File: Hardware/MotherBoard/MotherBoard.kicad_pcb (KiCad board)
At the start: 2 copper layers, 233.7 x 165.1 mm, 39 parts, among them J1 POWER, J10 I/O_PWR, J2 I/O0, J3 ISA00, J4 ISA10, J5 I/O1, J6 EXTRN_CLCK, J7 ISA01, J8 ISA11, J9 Conn_02x02_Odd_Even, SW1 SW_Push, U1 AMS1117-5.0, U2 28C256, U3 WD65C22, U4 HM62256BLP, U5 WD65C02, U6 4012, U7 4023, U8 4069, X1 ACO-1MHz

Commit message: Add buffers to extenstion ports
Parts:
- added U10: 74HCT541, Package_DIP:DIP-20_W7.62mm, F.Cu at (202.9, 26.7)
- added U11: SN74LVC245AN, Package_DIP:DIP-20_W7.62mm, F.Cu at (203.7, -35.6)
- added U12: SN74LVC245AN, Package_DIP:DIP-20_W7.62mm, F.Cu at (-40.9, -7.11)
- added U13: 74HCT541, Package_DIP:DIP-20_W7.62mm, F.Cu at (-39.9, 25.4)
- added U14: 74HCT541, Package_DIP:DIP-20_W7.62mm, F.Cu at (-41.1, -40.4)
- added U9: 74HCT541, Package_DIP:DIP-20_W7.62mm, F.Cu at (202.7, -5.08)
- moved Xiaoniuniu 217.4 mm to (37.6, 45.7)
- moved U2 101.2 mm to (128.8, 73.7)
- moved C6 101.2 mm to (146.8, 73.7)
- moved H4 80.1 mm to (166.0, 148.0)
- moved D1 77.0 mm to (128.8, 45.2)
- moved R4 77.0 mm to (128.8, 36.3)
- moved C1 77.0 mm to (154.2, 59.2)
- moved C2 77.0 mm to (133.9, 59.2)
- moved F1 77.0 mm to (161.8, 54.1)
- moved FB1 77.0 mm to (161.8, 66.8)
- moved J1 77.0 mm to (156.7, 44.8)
- moved U1 77.0 mm to (141.5, 59.2)
- moved H1 75.7 mm to (166.0, 28.0)
- moved X1 58.8 mm to (61.0, 145.4)
- moved J6 58.8 mm to (81.3, 146.3)
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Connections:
- J3 pad 1: /D0 -> Net-(J3-Pad1)
- J3 pad 2: /D1 -> Net-(J3-Pad2)
- J3 pad 3: /D2 -> Net-(J3-Pad3)
- J3 pad 4: /D3 -> Net-(J3-Pad4)
- J3 pad 5: /D4 -> Net-(J3-Pad5)
- J3 pad 6: /D5 -> Net-(J3-Pad6)
- J3 pad 7: /D6 -> Net-(J3-Pad7)
- J3 pad 8: /D7 -> Net-(J3-Pad8)
- J4 pad 1: /D0 -> Net-(J4-Pad1)
- J4 pad 2: /D1 -> Net-(J4-Pad2)
- J4 pad 3: /D2 -> Net-(J4-Pad3)
- J4 pad 4: /D3 -> Net-(J4-Pad4)
- J4 pad 5: /D4 -> Net-(J4-Pad5)
- J4 pad 6: /D5 -> Net-(J4-Pad6)
- J4 pad 7: /D6 -> Net-(J4-Pad7)
- J4 pad 8: /D7 -> Net-(J4-Pad8)
- J7 pad 1: /A0 -> Net-(J7-Pad1)
- J7 pad 10: /A9 -> Net-(J7-Pad10)
- J7 pad 11: /A10 -> Net-(J7-Pad11)
- J7 pad 12: /A11 -> Net-(J7-Pad12)
- J7 pad 13: /A12 -> Net-(J7-Pad13)
- J7 pad 14: /A13 -> Net-(J7-Pad14)
- J7 pad 15: /A14 -> Net-(J7-Pad15)
- J7 pad 2: /A1 -> Net-(J7-Pad2)
- J7 pad 3: /A2 -> Net-(J7-Pad3)
- J7 pad 4: /A3 -> Net-(J7-Pad4)
- J7 pad 5: /A4 -> Net-(J7-Pad5)
- J7 pad 6: /A5 -> Net-(J7-Pad6)
- J7 pad 7: /A6 -> Net-(J7-Pad7)
- J7 pad 8: /A7 -> Net-(J7-Pad8)
- J7 pad 9: /A8 -> Net-(J7-Pad9)
- J8 pad 1: /A0 -> Net-(J8-Pad1)
- J8 pad 10: /A9 -> Net-(J8-Pad10)
- J8 pad 11: /A10 -> Net-(J8-Pad11)
- J8 pad 12: /A11 -> Net-(J8-Pad12)
- J8 pad 13: /A12 -> Net-(J8-Pad13)
- J8 pad 14: /A13 -> Net-(J8-Pad14)
- J8 pad 15: /A14 -> Net-(J8-Pad15)
- J8 pad 2: /A1 -> Net-(J8-Pad2)
- J8 pad 3: /A2 -> Net-(J8-Pad3)
- J8 pad 4: /A3 -> Net-(J8-Pad4)
- J8 pad 5: /A4 -> Net-(J8-Pad5)
- J8 pad 6: /A5 -> Net-(J8-Pad6)
- J8 pad 7: /A6 -> Net-(J8-Pad7)
- J8 pad 8: /A7 -> Net-(J8-Pad8)
- J8 pad 9: /A8 -> Net-(J8-Pad9)
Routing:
- net /D2: track 572.3 -> 228.5 mm, vias 6 -> 4
- net /D1: track 569.8 -> 226.2 mm, vias 6 -> 4
- net /D0: track 567.2 -> 224.0 mm, vias 6 -> 4
- net /D7: track 529.5 -> 275.5 mm, vias 8 -> 6
- net /D3: track 571.9 -> 319.9 mm
- net /D6: track 511.6 -> 268.1 mm, vias 8 -> 6
- net /D5: track 493.8 -> 261.1 mm, vias 8 -> 6
- net /D4: track 476.0 -> 253.4 mm, vias 8 -> 6
- net /A11: track 469.5 -> 250.4 mm, vias 8 -> 5
- net /A10: track 478.2 -> 261.9 mm, vias 9 -> 5
- net RW: track 429.4 -> 235.0 mm, vias 5 -> 4
- net /A9: track 382.1 -> 190.9 mm, vias 6 -> 4
- net /A13: track 370.6 -> 180.2 mm, vias 7 -> 3
- net /A8: track 377.0 -> 191.7 mm, vias 6 -> 4
- net +5V: track 844.4 -> 659.9 mm, vias 7 -> 1
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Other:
- board size 233.7 x 165.1 mm -> 145 x 130.1 mm

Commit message: Fix
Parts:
- moved U12 125.0 mm to (77.0, 34.3)
- moved U14 111.8 mm to (43.1, 33.0)
- moved U11 92.3 mm to (141.9, 33.0)
- moved U9 90.8 mm to (120.2, 33.0)
- moved U13 90.4 mm to (43.2, 61.0)
- moved U10 72.1 mm to (131.1, 33.0)
- moved Xiaoniuniu 64.7 mm to (48.5, 109.5)
- moved C3 41.0 mm to (83.8, 132.1)
- moved C4 41.0 mm to (60.7, 140.0)
- moved C5 41.0 mm to (37.6, 170.2)
- moved X1 41.0 mm to (55.9, 186.0)
- moved F1 41.0 mm to (156.7, 94.7)
- moved C1 41.0 mm to (149.1, 99.8)
- moved C2 41.0 mm to (128.8, 99.8)
- moved C6 41.0 mm to (141.7, 114.3)
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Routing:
- net PORT1B: track 197.3 -> 315.3 mm
- net /D7: track 275.5 -> 390.8 mm, vias 6 -> 8
- net /D6: track 268.1 -> 379.5 mm, vias 6 -> 8
- net /D5: track 261.1 -> 366.8 mm, vias 6 -> 8
- net /D4: track 253.4 -> 353.6 mm, vias 6 -> 8
- net /D2: track 228.5 -> 317.6 mm, vias 4 -> 6
- net /D1: track 226.2 -> 309.7 mm, vias 4 -> 6
- net /D3: track 319.9 -> 398.7 mm, vias 6 -> 8
- net /D0: track 224.0 -> 301.8 mm, vias 4 -> 6
- net /A7: track 184.1 -> 254.9 mm, vias 4 -> 6
- net /A6: track 189.2 -> 255.2 mm, vias 4 -> 6
- net /A5: track 194.3 -> 255.5 mm, vias 4 -> 6
- net /A4: track 199.4 -> 255.8 mm, vias 4 -> 6
- net RW: track 235.0 -> 289.3 mm, vias 4 -> 6
- net /A12: track 178.8 -> 226.3 mm, vias 3 -> 5
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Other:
- board size 145 x 130.1 mm -> 145 x 164.8 mm

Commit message: Complete buffred extension ports
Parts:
- moved Xiaoniuniu 95.8 mm to (142.5, 90.9)
- moved U10 45.9 mm to (91.8, 56.8)
- moved R4 33.8 mm to (132.8, 44.4)
- moved D1 32.7 mm to (132.8, 54.4), turned to 180 degrees
- moved J1 32.0 mm to (154.5, 53.6)
- moved F1 31.8 mm to (160.8, 63.2)
- moved C1 31.8 mm to (153.2, 68.3)
- moved U1 31.8 mm to (140.5, 68.3)
- moved C2 31.8 mm to (132.6, 68.3)
- moved FB1 31.6 mm to (160.8, 76.1)
- moved U9 28.7 mm to (91.8, 28.8)
- moved U11 25.0 mm to (117.1, 30.1)
- moved H3 8.91 mm to (28.1, 180.0)
- moved H4 8.91 mm to (163.1, 180.0)
- moved C3 8.03 mm to (86.4, 124.5)
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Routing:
- net PORT2B: track 96.3 -> 212.8 mm
- net RW: track 289.3 -> 353.3 mm, vias 6 -> 7
- net /A0: track 298.8 -> 360.4 mm, vias 9 -> 10
- net /A1: track 298.0 -> 358.7 mm, vias 9 -> 11
- net +5V: track 691.6 -> 751.4 mm, vias 2 -> 1
- net /A2: track 299.7 -> 359.2 mm, vias 8 -> 10
- net /A3: track 300.4 -> 359.1 mm, vias 8 -> 10
- net /A4: track 255.8 -> 313.3 mm, vias 6 -> 8
- net /A5: track 255.5 -> 312.0 mm, vias 6 -> 8
- net /A6: track 255.2 -> 310.7 mm, vias 6 -> 8
- net /A7: track 254.9 -> 309.4 mm, vias 6 -> 8
- net RESET: track 196.9 -> 236.7 mm
- net /A8: track 233.9 -> 272.8 mm, vias 6 -> 8
- net CLOCK: track 202.3 -> 241.1 mm
- net /A9: track 233.4 -> 269.7 mm, vias 6 -> 8
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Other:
- board size 145 x 164.8 mm -> 145 x 160 mm
- board text added: "PORT2B"
- board text removed: "PORT1A"

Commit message: Fix
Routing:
- net +5V: track 751.4 -> 750.5 mm
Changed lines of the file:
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@@
   (segment (start 145.542 68.3255) (end 145.542 73.4055) (width 0.3) (layer "F.Cu") (net 2))
   (segment (start 98.044 55.372) (end 99.441 56.769) (width 0.5) (layer "F.Cu") (net 3))
-  (segment (start 127.2545 54.3555) (end 127.254 54.356) (width 0.5) (layer "F.Cu") (net 3))
   (segment (start 77.979853 30.083285) (end 81.012138 27.051) (width 0.5) (layer "F.Cu") (net 3))
   (segment (start 63.263 127.055831) (end 61.468 128.850831) (width 0.5) (layer "F.Cu") (net 3))
   (segment (start 52.74152 28.973999) (end 53.140519 28.575) (width 0.5) (layer "F.Cu") (net 3))
   (segment (start 50.545 162.56) (end 58.165 154.94) (width 0.5) (layer "F.Cu") (net 3))
+  (segment (start 127.2545 54.3555) (end 127.254 68.326) (width 0.5) (layer "F.Cu") (net 3))
   (segment (start 66.04 132.08) (end 78.74 132.08) (width 0.5) (layer "F.Cu") (net 3))
   (segment (start 81.28 124.46) (end 86.36 124.46) (width 0.5) (layer "F.Cu") (net 3))
   (segment (start 86.36 124.46) (end 88.9 124.46) (width 0.5) (layer "F.Cu") (net 3))
   (segment (start 81.28 124.46) (end 80.01 124.46) (width 0.5) (layer "F.Cu") (net 3))
-  (segment (start 146.05 153.416) (end 146.05 154.178) (width 0.5) (layer "F.Cu") (net 3))
+  (segment (start 146.05 151.892) (end 146.05 154.178) (width 0.5) (layer "F.Cu") (net 3))
   (segment (start 80.01 124.46) (end 79.502 124.968) (width 0.5) (layer "F.Cu") (net 3))
   (segment (start 152.4 160.02) (end 152.4 157.48) (width 0.5) (layer "F.Cu") (net 3))
   (segment (start 133.8575 70.8655) (end 141.733 70.8655) (width 0.5) (layer "F.Cu") (net 3))
+  (segment (start 127.254 68.326) (end 127.254 101.092) (width 0.5) (layer "F.Cu") (net 3))
+  (segment (start 116.84 101.092) (end 127.254 101.092) (width 0.5) (layer "F.Cu") (net 3))
   (segment (start 88.9 101.092) (end 88.9 104.14) (width 0.5) (layer "F.Cu") (net 3))
   (segment (start 111.76 157.48) (end 111.76 155.194) (width 0.5) (layer "F.Cu") (net 3))
@@
   (segment (start 50.546 162.56) (end 58.42 170.763903) (width 0.5) (layer "F.Cu") (net 3))
   (segment (start 155.194 179.832) (end 153.416 181.61) (width 0.5) (layer "F.Cu") (net 3))
-  (segment (start 126.363147 68.214715) (end 110.226918 68.214715) (width 0.5) (layer "F.Cu") (net 3))
   (segment (start 116.84 106.68) (end 116.84 101.092) (width 0.5) (layer "F.Cu") (net 3))
   (segment (start 116.84 106.68) (end 119.651 106.68) (width 0.5) (layer "F.Cu") (net 3))
@@
   (segment (start 123.078715 28.590715) (end 124.714 30.099) (width 0.5) (layer "F.Cu") (net 3))
   (segment (start 131.318 101.092) (end 136.906 106.68) (width 0.5) (layer "F.Cu") (net 3))
-  (segment (start 63.263 132.334) (end 63.517 132.08) (width 0.5) (layer "F.Cu") (net 3))
   (segment (start 149.098 154.178) (end 146.05 154.178) (width 0.5) (layer "F.Cu") (net 3))
+  (segment (start 127.363432 68.216568) (end 132.510578 68.216568) (width 0.5) (layer "F.Cu") (net 3))
   (segment (start 127.254 54.355) (end 127.254 32.639) (width 0.5) (layer "F.Cu") (net 3))
   (segment (start 81.026 181.61) (end 78.74 179.324) (width 0.5) (layer "F.Cu") (net 3))
   (segment (start 40.148 162.56) (end 42.925 162.56) (width 0.5) (layer "F.Cu") (net 3))
   (segment (start 90.424 122.936) (end 90.424 105.664) (width 0.5) (layer "F.Cu") (net 3))
+  (segment (start 127.254 101.092) (end 131.318 101.092) (width 0.5) (layer "F.Cu") (net 3))
   (segment (start 81.012138 27.051) (end 97.663 27.051) (width 0.5) (layer "F.Cu") (net 3))
   (segment (start 130.302 54.3555) (end 127.2545 54.3555) (width 0.5) (layer "F.Cu") (net 3))
@@
   (segment (start 153.416 181.61) (end 81.026 181.61) (width 0.5) (layer "F.Cu") (net 3))
   (segment (start 79.502 131.318) (end 78.74 132.08) (width 0.5) (layer "F.Cu") (net 3))
-  (segment (start 126.365 68.216568) (end 132.510578 68.216568) (width 0.5) (layer "F.Cu") (net 3))
   (segment (start 63.517 132.08) (end 65.532 132.08) (width 0.5) (layer "F.Cu") (net 3))
-  (segment (start 126.363147 68.214715) (end 126.365 68.216568) (width 0.5) (layer "F.Cu") (net 3))
   (segment (start 141.478 106.68) (end 144.289 106.68) (width 0.5) (layer "F.Cu") (net 3))
   (segment (start 99.747666 28.590715) (end 123.078715 28.590715) (width 0.5) (layer "F.Cu") (net 3))
@@
   (segment (start 61.468 130.539) (end 63.263 132.334) (width 0.5) (layer "F.Cu") (net 3))
   (segment (start 127.2545 54.3555) (end 127.254 54.355) (width 0.5) (layer "F.Cu") (net 3))
-  (segment (start 65.532 132.08) (end 66.04 132.08) (width 0.5) (layer "F.Cu") (net 3))
   (segment (start 111.76 155.194) (end 112.776 154.178) (width 0.5) (layer "F.Cu") (net 3))
   (segment (start 61.468 128.850831) (end 61.468 130.539) (width 0.5) (layer "F.Cu") (net 3))
@@
   (segment (start 132.08 157.48) (end 132.08 160.02) (width 0.5) (layer "F.Cu") (net 3))
   (segment (start 132.588 68.29399) (end 132.588 69.596) (width 0.5) (layer "F.Cu") (net 3))
+  (segment (start 110.226918 68.214715) (end 127.363432 68.216568) (width 0.5) (layer "F.Cu") (net 3))
   (segment (start 76.471568 28.575) (end 77.979853 30.083285) (width 0.5) (layer "F.Cu") (net 3))
   (segment (start 58.42 170.763903) (end 70.358 170.763903) (width 0.5) (layer "F.Cu") (net 3))
   (segment (start 97.663 27.051) (end 99.441 28.829) (width 0.5) (layer "F.Cu") (net 3))
-  (segment (start 127.254 54.356) (end 127.363432 68.216568) (width 0.5) (layer "F.Cu") (net 3))
   (segment (start 111.76 157.48) (end 113.284 159.004) (width 0.5) (layer "F.Cu") (net 3))
   (segment (start 70.358 170.763903) (end 78.74 179.324) (width 0.5) (layer "F.Cu") (net 3))
-  (segment (start 127.363432 68.216568) (end 127.508 101.092) (width 0.5) (layer "F.Cu") (net 3))
-  (segment (start 146.05 151.892) (end 146.05 153.416) (width 0.5) (layer "F.Cu") (net 3))
   (segment (start 127.254 32.639) (end 124.714 30.099) (width 0.5) (layer "F.Cu") (net 3))
-  (segment (start 116.84 101.092) (end 131.318 101.092) (width 0.5) (layer "F.Cu") (net 3))
   (segment (start 90.424 105.664) (end 88.9 104.14) (width 0.5) (layer "F.Cu") (net 3))
-  (segment (start 144.289 106.68) (end 144.272 106.697) (width 0.5) (layer "F.Cu") (net 3))
   (segment (start 72.644 55.372) (end 98.044 55.372) (width 0.5) (layer "F.Cu") (net 3))
   (segment (start 136.906 106.68) (end 141.478 106.68) (width 0.5) (layer "F.Cu") (net 3))

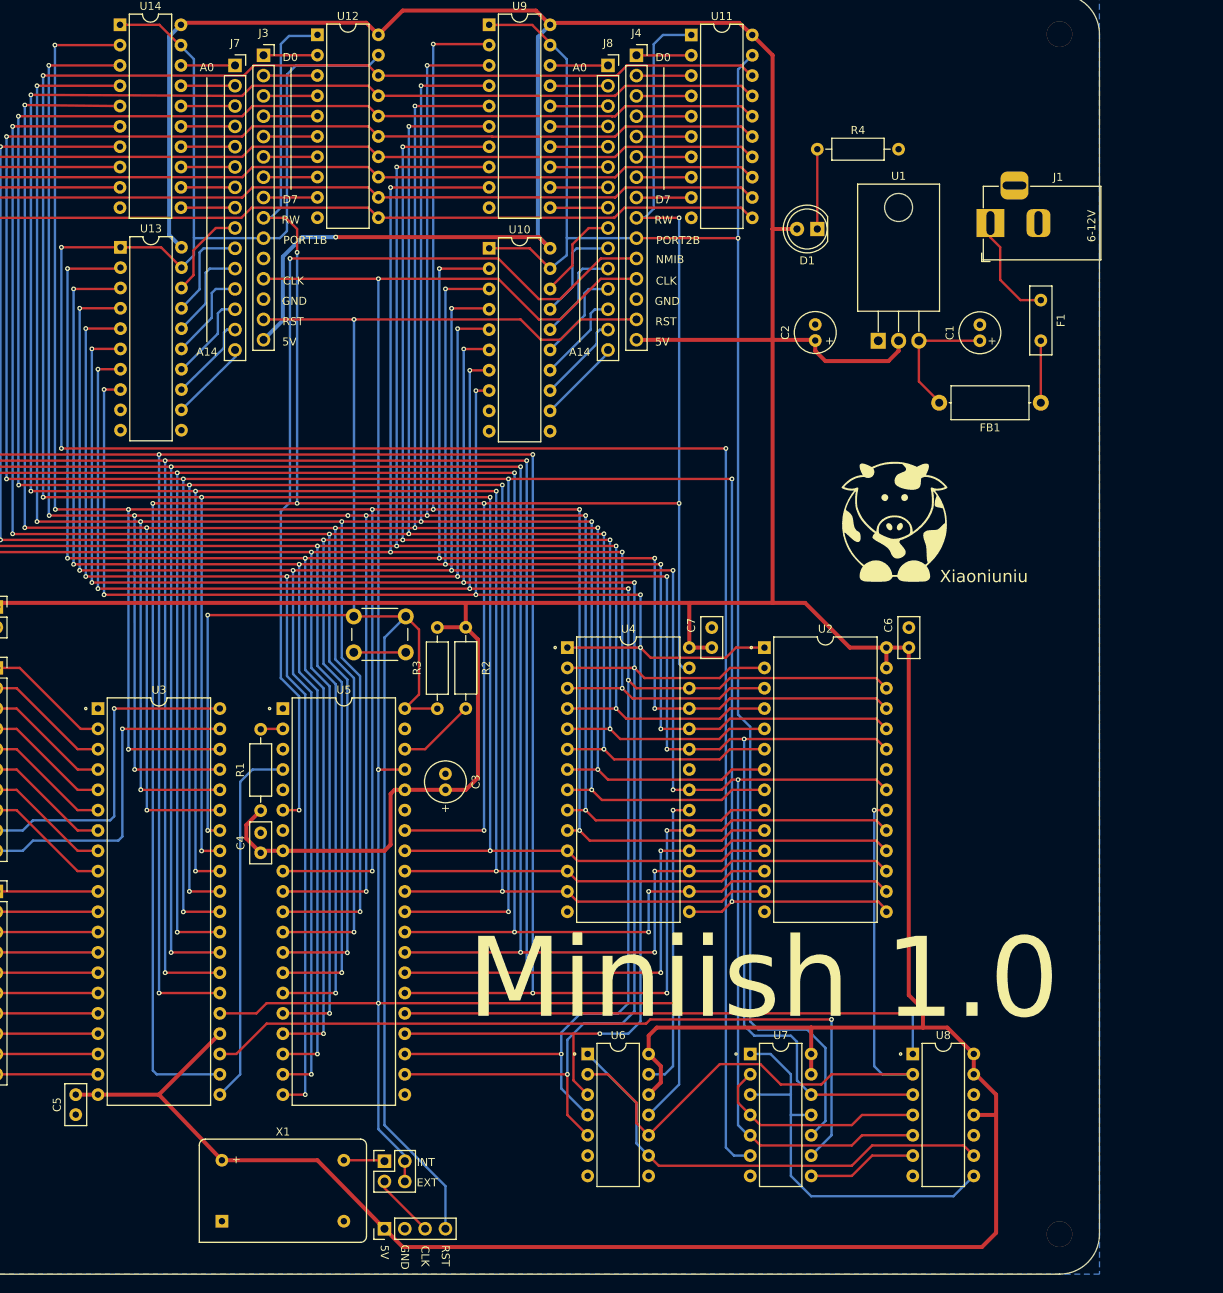
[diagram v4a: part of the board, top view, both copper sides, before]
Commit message: Replace logic IC 4xxx by 74hcxx
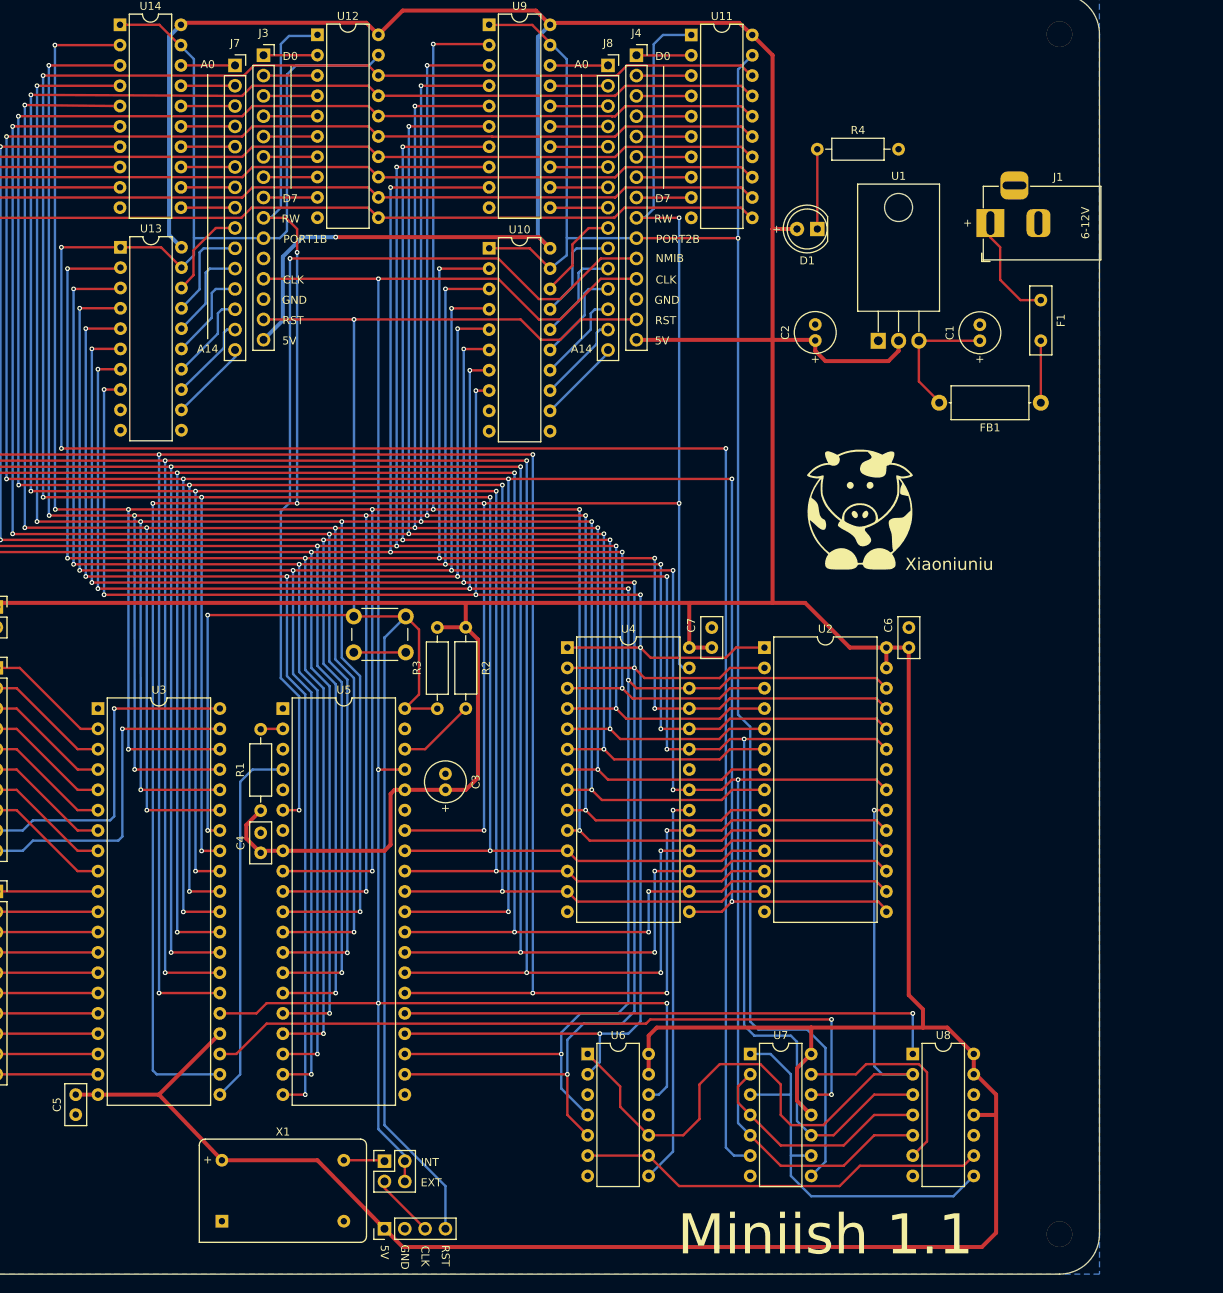
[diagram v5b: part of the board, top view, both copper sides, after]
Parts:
- U6: value 4012 -> 74HC20
- U7: value 4023 -> 74HC10
- U8: value 4069 -> 74HC04
- moved Xiaoniuniu 4.58 mm to (138.2, 89.4)
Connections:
- net NMIB renamed /NMIB
- net PORT1B renamed /PORT1B
- net RW renamed /RW
- J3 pad 12: CLOCK -> /CLOCK
- J4 pad 10: PORT2B -> /PORT2B
- J4 pad 12: CLOCK -> /CLOCK
- J9 pad 2: CLOCK -> /CLOCK
- J9 pad 4: CLOCK -> /CLOCK
- U10 pad 1: PORT2B -> /PORT2B
- U10 pad 19: PORT2B -> /PORT2B
- U11 pad 19: PORT2B -> /PORT2B
- U3 pad 25: CLOCK -> /CLOCK
- U5 pad 37: CLOCK -> /CLOCK
- U6 pad 1: Net-(U6-Pad1) -> /ROMCSB
- U6 pad 11: CLOCK -> (no net)
- U6 pad 12: +5V -> /CLOCK
- U6 pad 13: /RAMCSB -> +5V
- U6 pad 2: /ROMCSB -> /A14
- U6 pad 3: /A14 -> (no net)
- U6 pad 6: (no net) -> Net-(U6-Pad6)
- U6 pad 8: (no net) -> /RAMCSB
- U6 pad 9: Net-(U6-Pad1) -> Net-(U6-Pad6)
- U7 pad 10: PORT2B -> /A11
- U7 pad 11: Net-(U7-Pad1) -> +5V
- U7 pad 12: /A11 -> /IOCSB
- U7 pad 13: +5V -> Net-(U7-Pad13)
- U7 pad 8: Net-(U7-Pad8) -> /PORT2B
- U7 pad 9: /IOCSB -> Net-(U7-Pad1)
- U8 pad 6: Net-(U7-Pad8) -> Net-(U7-Pad13)
- U8 pad 9: Net-(U6-Pad1) -> Net-(U6-Pad6)
- U9 pad 1: PORT2B -> /PORT2B
- U9 pad 19: PORT2B -> /PORT2B
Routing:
- net CLOCK: track 241.1 -> 0.00 mm, vias 4 -> 0
- net /CLOCK: track 0.00 -> 237.2 mm, vias 0 -> 4
- net /PORT2B: track 0.00 -> 217.9 mm, vias 0 -> 1
- net PORT2B: track 212.8 -> 0.00 mm, vias 1 -> 0
- net Net-(U6-Pad1): track 58.6 -> 0.00 mm
- net Net-(U6-Pad6): track 0.00 -> 51.4 mm
- net Net-(U7-Pad13): track 0.00 -> 26.6 mm
- net Net-(U7-Pad8): track 13.8 -> 0.00 mm
- net /RAMCSB: track 37.5 -> 49.0 mm
- net /ROMCSB: track 89.3 -> 99.3 mm
- net /A11: track 324.6 -> 331.8 mm
- net /IOCSB: track 96.3 -> 90.2 mm, vias 1 -> 2
- net +5V: track 750.5 -> 753.3 mm
- net /A14: track 239.4 -> 236.7 mm
- net /A10: track 338.4 -> 340.6 mm
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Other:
- board text added: "Miniish 1.1"
- board text removed: "Miniish 1.0"

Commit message: Finalize daughter board
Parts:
- added C8: 470nF, Capacitor_THT:C_Disc_D5.0mm_W2.5mm_P2.50mm, F.Cu at (85.3, 117.9)
- SW1: value SW_Push -> RESET_SW
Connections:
- net Net-(J3-Pad11) renamed no_connect_115
- net Net-(U10-Pad11) renamed no_connect_116
- net Net-(U13-Pad11) renamed no_connect_117
- net Net-(U5-Pad1) renamed no_connect_118
- net Net-(U5-Pad3) renamed no_connect_119
- net Net-(U5-Pad35) renamed no_connect_120
- net Net-(U5-Pad39) renamed no_connect_121
- net Net-(U5-Pad5) renamed no_connect_122
- net Net-(U5-Pad7) renamed no_connect_123
- net Net-(U8-Pad10) renamed no_connect_124
- net Net-(U8-Pad12) renamed no_connect_125
- net Net-(X1-Pad1) renamed no_connect_126
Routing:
- net RESET: track 236.7 -> 240.3 mm
- net Net-(R2-Pad2): track 9.72 -> 12.6 mm
